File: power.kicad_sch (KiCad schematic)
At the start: 41 parts, among them J1 POWER_IN, J2 POWER_OUT, Q1 SUD50P10-43L-GE3, Q2 SUD50P10-43L-GE3, Q3 SUD50P10-43L-GE3, U12 +3V3@2A, U9 +5V@2A

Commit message: more cleanup and added notes for review
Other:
- note added: "ADD FERRITES?"
- note added: "DO WE HAVE AN INTERNAL TEMP SENSOR?"
- note added: "FUSE OUTPUTS"
- note added: "INCREASE BULK CAPACTORS AND GET 100V RATED"
- note added: "OR ADD CURRENT SENSOR"
- note removed: "These power..."

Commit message: DNP unused connectors for now
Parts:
- J2: now not fitted
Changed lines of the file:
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@@
 		(in_bom yes)
 		(on_board yes)
-		(dnp no)
+		(dnp yes)
 		(property "Reference" "J2"
 			(at 231.902 132.842 0)

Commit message: pcb review session notes
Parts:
- J2: now fitted
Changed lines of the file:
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@@
 	(text "ADD FERRITES?\n"
 		(exclude_from_sim no)
-		(at 28.5927 76.2834 0)
+		(at 17.526 68.58 0)
 		(effects
 			(font
@@
 	(text "OR ADD CURRENT SENSOR"
 		(exclude_from_sim no)
-		(at 199.898 166.878 0)
+		(at 180.086 162.56 0)
 		(effects
 			(font
@@
 	(text "INCREASE BULK CAPACTORS\nAND GET 100V RATED"
 		(exclude_from_sim no)
-		(at 123.19 74.93 0)
+		(at 132.842 40.386 0)
 		(effects
 			(font
@@
 		(in_bom yes)
 		(on_board yes)
-		(dnp yes)
+		(dnp no)
 		(property "Reference" "J2"
 			(at 231.902 132.842 0)

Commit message: major rework again after the meeting
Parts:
- removed C1, C11, C12, C13, C2, C3, C4: 0.1 uF, Capacitor_SMD:C_1206_3216Metric_Pad1.33x1.80mm_HandSolder, symbol Device:C
- removed C10, C5: 22 uF, Payload_PCB_v3.1:UCM1H220MCL1GS, symbol Device:C_Polarized_US
- removed D2, D3: BZT52C10-TP, Diode_SMD:D_SOD-123, symbol Device:D_Zener
- removed F2, F3: Fuse, Fuse:Fuseholder_Blade_Mini_Keystone_3568, symbol Device:Fuse
- removed JP1, JP2, JP3, JP4: SolderJumper_2_Open, Jumper:SolderJumper-2_P1.3mm_Open_RoundedPad1.0x1.5mm, symbol Jumper:SolderJumper_2_Open
- removed Q2, Q3: SUD50P10-43L-GE3, Package_TO_SOT_SMD:TO-252-2, symbol Device:Q_PMOS_GDS
- removed TP2: +BATT_IN, TestPoint:TestPoint_Pad_D2.0mm, symbol Connector:TestPoint
- removed TP3: +VDC_IN, TestPoint:TestPoint_Pad_D2.0mm, symbol Connector:TestPoint
- removed TP4, TP6: +12V_IN, TestPoint:TestPoint_Pad_D2.0mm, symbol Connector:TestPoint
- added C1: 22 uF, Capacitor_THT:CP_Radial_D10.0mm_P5.00mm, symbol Device:C_Polarized_US
- added D2, D3, D5: +12V, LED_SMD:LED_0805_2012Metric_Pad1.15x1.40mm_HandSolder, symbol Device:LED
- added Q2: MMBT3904, Package_TO_SOT_SMD:SOT-23, symbol Transistor_BJT:MMBT3904
- added R10, R8, R9: 45m, Resistor_SMD:R_1206_3216Metric_Pad1.30x1.75mm_HandSolder, symbol Device:R_US
- added R17: 511, Resistor_SMD:R_0603_1608Metric_Pad0.98x0.95mm_HandSolder, symbol Device:R_US
- added U3: LTC2990, Package_SO:MSOP-10_3x3mm_P0.5mm, symbol Sensor:LTC2990
- C9: value 0.1 uF -> 470p; footprint Capacitor_SMD:C_1206_3216Metric_Pad1.33x1.80mm_HandSolder -> Capacitor_SMD:C_0603_1608Metric_Pad1.08x0.95mm_HandSolder
- F1: footprint Fuse:Fuseholder_Blade_Mini_Keystone_3568 -> Fuse:Fuse_1210_3225Metric
- J1: footprint Connector_Molex:Molex_Mini-Fit_Jr_5569-06A2_2x03_P4.20mm_Horizontal -> Connector_Molex:Molex_Micro-Fit_3.0_43045-0200_2x01_P3.00mm_Horizontal; symbol Connector_Generic:Conn_02x03_Counter_Clockwise -> Connector_Generic:Conn_01x02; Manufacturer (none) -> Molex; Manufacturer Part Number (none) -> 0430450200; Vendor (none) -> Digikey; Vendor Part Number (none) -> WM1813-ND
- J2: footprint Connector_Molex:Molex_Mini-Fit_Jr_5569-12A2_2x06_P4.20mm_Horizontal -> Connector_Molex:Molex_Micro-Fit_3.0_43045-0600_2x03_P3.00mm_Horizontal; symbol Connector_Generic:Conn_02x06_Counter_Clockwise -> Connector_Generic:Conn_02x03_Top_Bottom; Manufacturer (none) -> Molex; Manufacturer Part Number (none) -> 0430450602; Vendor (none) -> Digikey; Vendor Part Number (none) -> WM1821-ND
- R3, R4: value 100k -> 511; footprint Resistor_SMD:R_0805_2012Metric_Pad1.20x1.40mm_HandSolder -> Resistor_SMD:R_0603_1608Metric_Pad0.98x0.95mm_HandSolder
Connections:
- net +12V: now also J2.4 (Pin_4), C1.1, R10.2, R17.2, R8.2, R9.2, U3.2 (V2); no longer D1.1 (K), J2.8 (Pin_8), J2.9 (Pin_9), Q1.3 (S)
- net +12V_IN: now also J1.2 (Pin_2); no longer J1.6 (Pin_6)
- net +3.3V: now also J2.6 (Pin_6), R4.2; no longer J2.11 (Pin_11)
- net +5V: now also J2.5 (Pin_5), R3.2; no longer J2.10 (Pin_10)
- net GND: now also C1.2, D2.1 (K), D3.1 (K), D5.1 (K), U3.5 (GND), U3.8 (ADR0), U3.9 (ADR1); no longer C9.1, J1.2 (Pin_2), J1.3 (Pin_3), J2.4 (Pin_4), J2.5 (Pin_5), J2.6 (Pin_6), R3.2, R4.2
- net at R4.1: now also D3.2 (A)
- net at R3.1: now also D2.2 (A)
- net +BATT: no longer names the net of C9.2
- net +BATT: now also Q2.1 (B), Q2.3 (C), U3.3 (V3); no longer J2.7 (Pin_7)
- removed net +BATT_IN: J1.5 (Pin_5)
- removed net VDC: J2.12 (Pin_12)
- new net: D5.2 (A), R17.1
- new net: C9.1, Q2.2 (E), U3.4 (V4)
- new net +12V_PROTECTED: D1.1 (K), Q1.3 (S), R10.1, R8.1, R9.1, U3.1 (V1)
- new net I2C0_SCL: U3.7 (SCL)
- new net I2C0_SDA: U3.6 (SDA)
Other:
- note added: "BULK CAPACITOR"
- note added: "CURRENT AND TEMPERATURE MONITOR"
- note removed: "+VDC is the servo voltage."
- note removed: "ADD FERRITES?"
- note removed: "Additional voltage input option or extra 40V input."
- note removed: "Bulk Decoupling"
- note removed: "DO WE HAVE AN INTERNAL TEMP SENSOR?"
- note removed: "FUSE OUTPUTS"
- note removed: "Fuse Protection"
- note removed: "INCREASE BULK CAPACTORS AND GET 100V RATED"
- note removed: "Note that these voltages are protected."
- note removed: "OR ADD CURRENT SENSOR"
- note removed: "Reverse-voltage protection"
- note removed: "The main power source is the +12V in. The other voltages are fed directly back out and are unused by any onboard components."
- moved on the sheet: D1, F1, Q1, R2, TP1, TP10, TP11, TP5, TP7, TP8, TP9, U12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

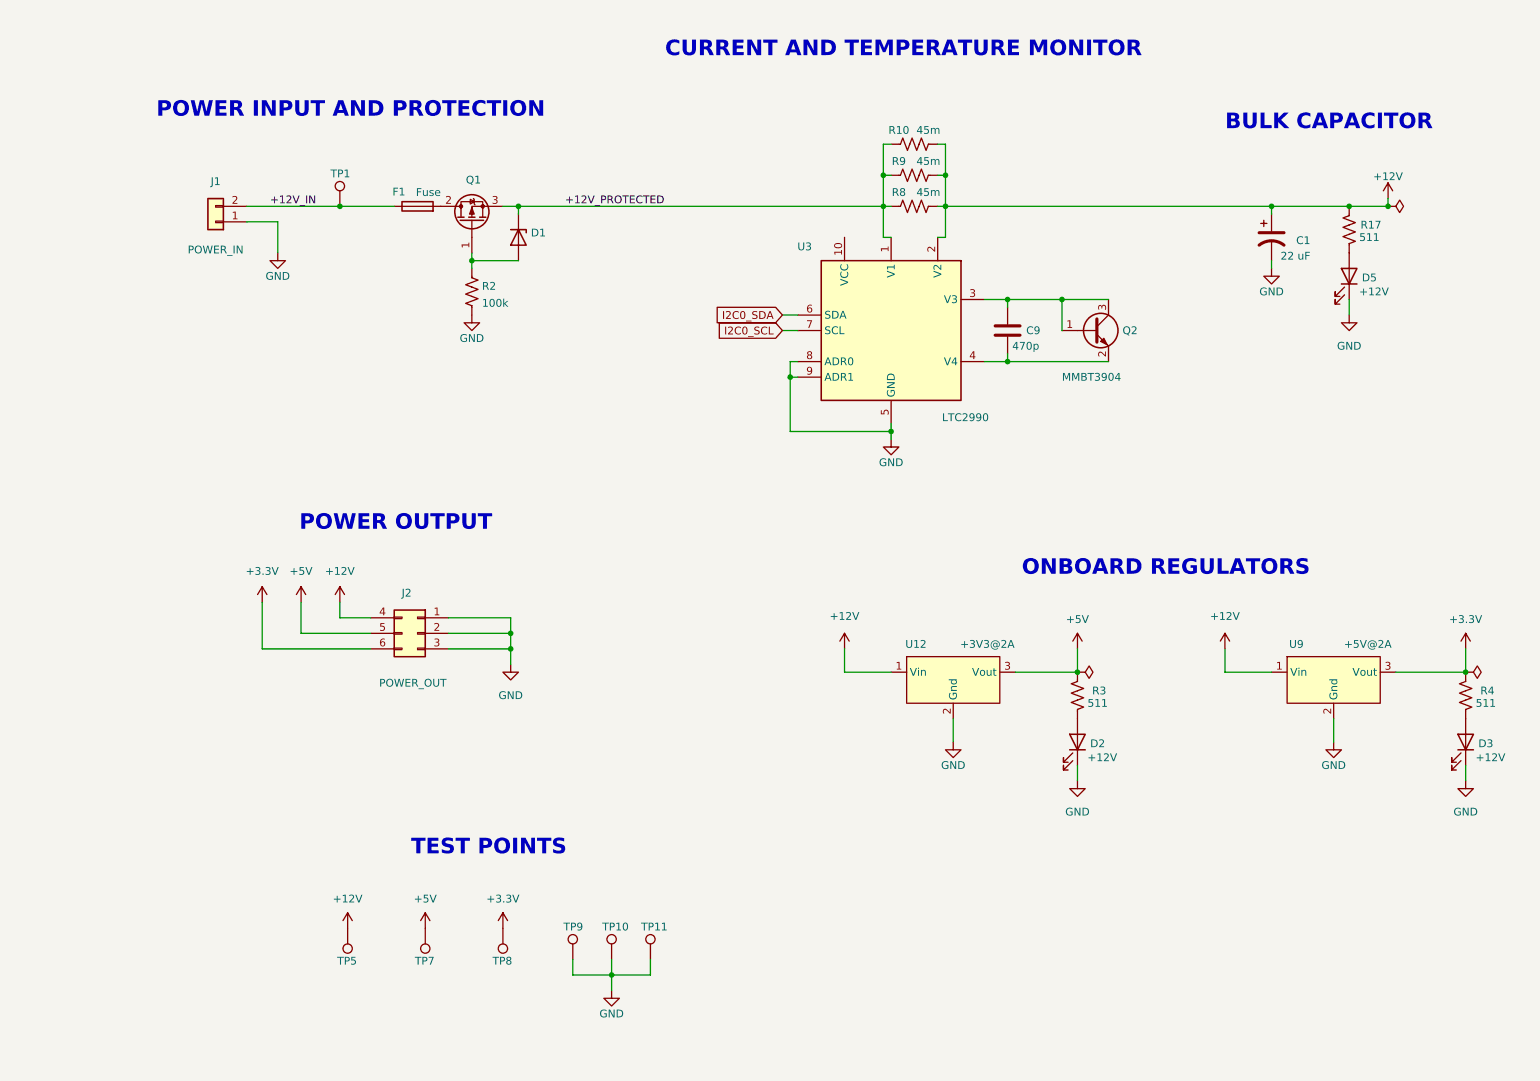
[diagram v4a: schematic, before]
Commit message: major finishing touches:     - major rework for v5.1     - silkscreen and stuff     - impednace for USB and CAN lines     - schematic comments     - symbol, footprint, and model library updates
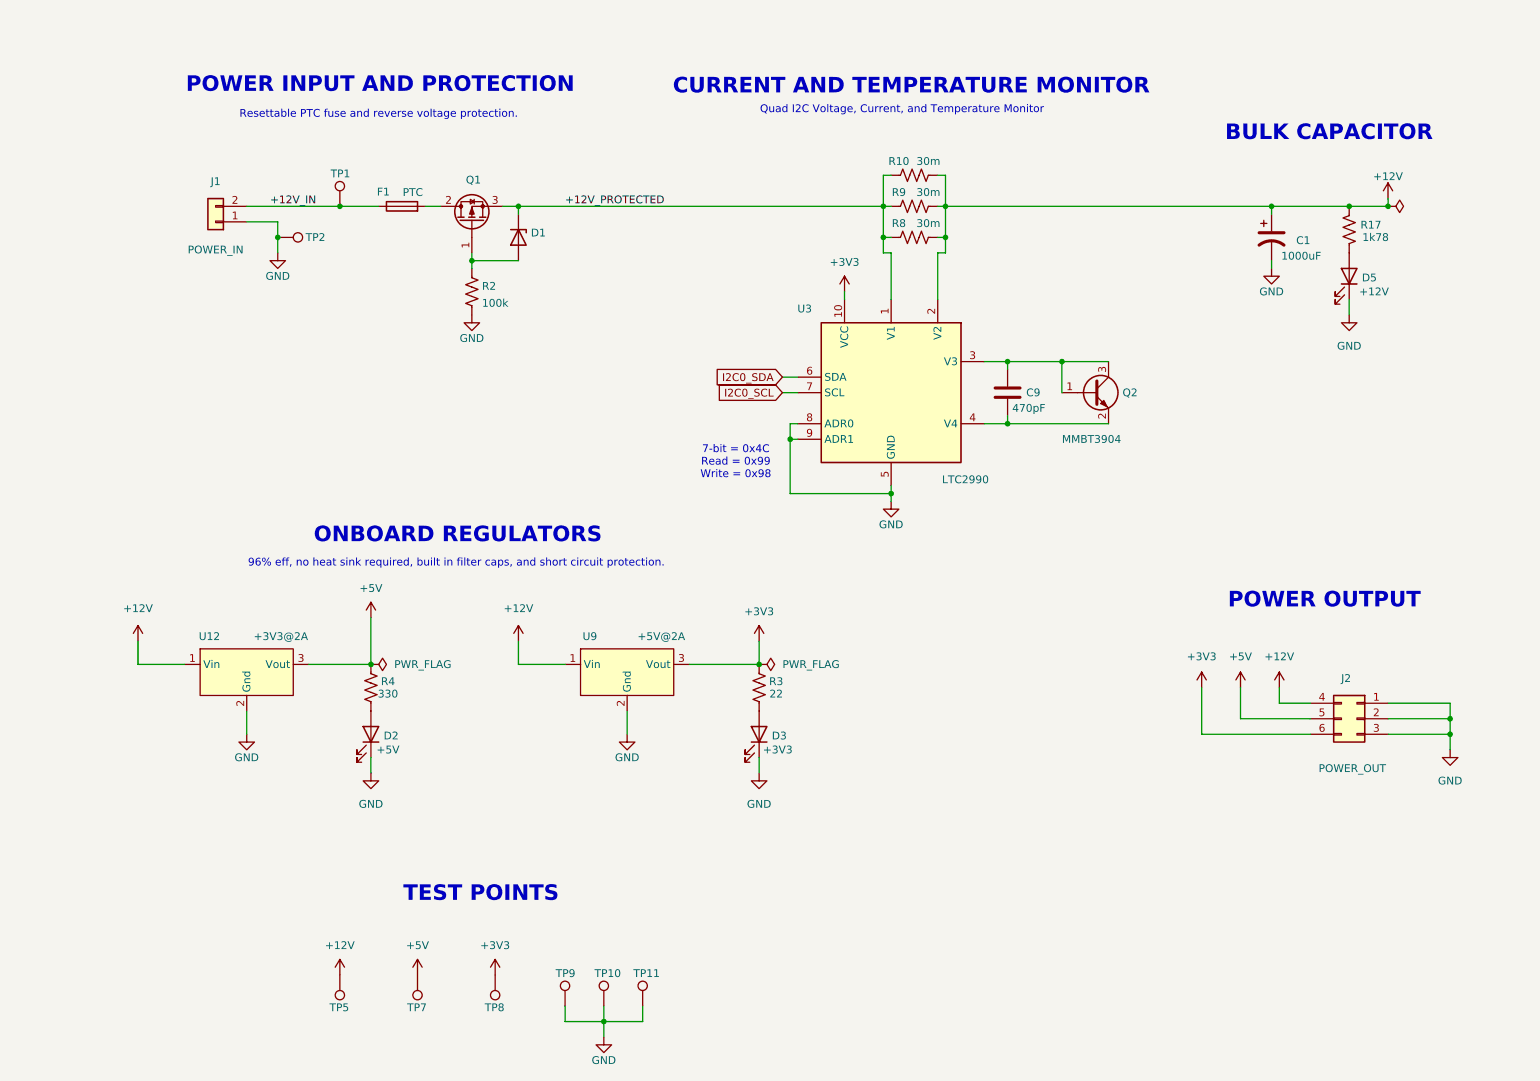
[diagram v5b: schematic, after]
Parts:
- added TP2: GND, TestPoint:TestPoint_Pad_D2.0mm, symbol Connector:TestPoint
- C1: value 22 uF -> 1000uF; Manufacturer (none) -> Nichicon; Manufacturer Part Number (none) -> UVR1E102MPD; Vendor (none) -> Digikey; Vendor Part Number (none) -> 493-1065-ND
- C9: value 470p -> 470pF; Manufacturer (none) -> KEMET; Manufacturer Part Number (none) -> C0603C471K5RACTU; Vendor (none) -> Digikey; Vendor Part Number (none) -> 399-C0603C471K5RACTUCT-ND
- D1: Manufacturer (none) -> MCC (Micro Commercial Components); Manufacturer Part Number (none) -> BZT52C10-TP; Vendor (none) -> Digikey; Vendor Part Number (none) -> BZT52C10-TPMSCT-ND
- D2: value +12V -> +5V; Manufacturer (none) -> Würth Elektronik; Manufacturer Part Number (none) -> 150080GS75000; Vendor (none) -> Digikey; Vendor Part Number (none) -> 732-4983-1-ND
- D3: value +12V -> +3V3; Manufacturer (none) -> Würth Elektronik; Manufacturer Part Number (none) -> 150080GS75000; Vendor (none) -> Digikey; Vendor Part Number (none) -> 732-4983-1-ND
- D5: Manufacturer (none) -> Würth Elektronik; Manufacturer Part Number (none) -> 150080GS75000; Vendor (none) -> Digikey; Vendor Part Number (none) -> 732-4983-1-ND
- F1: value Fuse -> PTC; Manufacturer (none) -> Littelfuse Inc.; Manufacturer Part Number (none) -> 1210L150/16WR; Vendor (none) -> Digikey; Vendor Part Number (none) -> F6135CT-ND
- Q1: symbol Device:Q_PMOS_GDS -> Transistor_FET:Q_PMOS_GDS; Manufacturer (none) -> Vishay Siliconix; Manufacturer Part Number (none) -> SUD50P10-43L-GE3; Vendor (none) -> Digikey; Vendor Part Number (none) -> SUD50P10-43L-GE3CT-ND
- Q2: Manufacturer (none) -> onsemi; Manufacturer Part Number (none) -> MMBT3904LT1G; Vendor (none) -> Digikey; Vendor Part Number (none) -> MMBT3904LT1GOSCT-ND
- R10, R8, R9: value 45m -> 30m; Manufacturer (none) -> Stackpole Electronics Inc; Manufacturer Part Number (none) -> CSR1206FT30L0; Vendor (none) -> Digikey; Vendor Part Number (none) -> 738-CSR1206FT30L0CT-ND
- R17: value 511 -> 1k78; Manufacturer (none) -> Stackpole Electronics Inc; Manufacturer Part Number (none) -> RNCP0603FTD1K78; Vendor (none) -> Digikey; Vendor Part Number (none) -> RNCP0603FTD1K78CT-ND
- R2: footprint Resistor_SMD:R_0805_2012Metric_Pad1.20x1.40mm_HandSolder -> Resistor_SMD:R_0603_1608Metric_Pad0.98x0.95mm_HandSolder; Manufacturer (none) -> Stackpole Electronics Inc; Manufacturer Part Number (none) -> RMCF0603FT100K; Vendor (none) -> Digikey; Vendor Part Number (none) -> RMCF0603FT100KCT-ND
- R3: value 511 -> 22; Manufacturer (none) -> Stackpole Electronics Inc; Manufacturer Part Number (none) -> RNCP0603FTD22R1; Vendor (none) -> Digikey; Vendor Part Number (none) -> RNCP0603FTD22R1CT-ND
- R4: value 511 -> 330; Manufacturer (none) -> Stackpole Electronics Inc; Manufacturer Part Number (none) -> RNCP0603FTD332R; Vendor (none) -> Digikey; Vendor Part Number (none) -> RNCP0603FTD332RCT-ND
- TP1: now left out of the parts list
- TP10, TP11, TP9: value +12V_IN -> GND; now left out of the parts list
- TP5: value +12V_IN -> +12V; now left out of the parts list
- TP7: value +12V_IN -> +5V; now left out of the parts list
- TP8: value +12V_IN -> +3V3; now left out of the parts list
- U12: symbol Regulators:173010542 -> symbols:TSR_2-2433; Manufacturer (none) -> Traco Power; Manufacturer Part Number (none) -> TSR 2-2433; Vendor (none) -> Digikey; Vendor Part Number (none) -> 1951-2426-ND
- U3: Manufacturer (none) -> Analog Devices Inc.; Manufacturer Part Number (none) -> LTC2990IMS#TRPBF; Vendor (none) -> Digikey; Vendor Part Number (none) -> 505-LTC2990IMS#TRPBFCT-ND
- U9: symbol Regulators:173010542 -> symbols:TSR_2-2450; Manufacturer (none) -> Traco Power; Manufacturer Part Number (none) -> TSR 2-2450; Vendor (none) -> Digikey; Vendor Part Number (none) -> 1951-2692-ND
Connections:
- net +5V: now also R4.2; no longer R3.2
- net GND: now also TP2.1
- net at R4.1: now also D2.2 (A); no longer D3.2 (A)
- net at R3.1: now also D3.2 (A); no longer D2.2 (A)
- net +3V3: now reaches U3.10 (VCC)
- net +3V3: now also J2.6 (Pin_6), R3.2, TP8.1, U9.3 (Vout)
- removed net +3.3V: J2.6 (Pin_6), R4.2, TP8.1, U9.3 (Vout)
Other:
- note added: "7-bit = 0x4C Read = 0x99 Write = 0x98"
- note added: "96% eff, no heat sink required, built in filter caps, and short circuit protection."
- note added: "Quad I2C Voltage, Current, and Temperature Monitor"
- note added: "Resettable PTC fuse and reverse voltage protection."
- company: WVU Unviersity Rover Challenge -> WVU Unviersity Rover Challenge (URC)
- moved on the sheet: C9, D2, D3, F1, J2, Q2, R10, R8, R9, TP10, TP11, TP5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

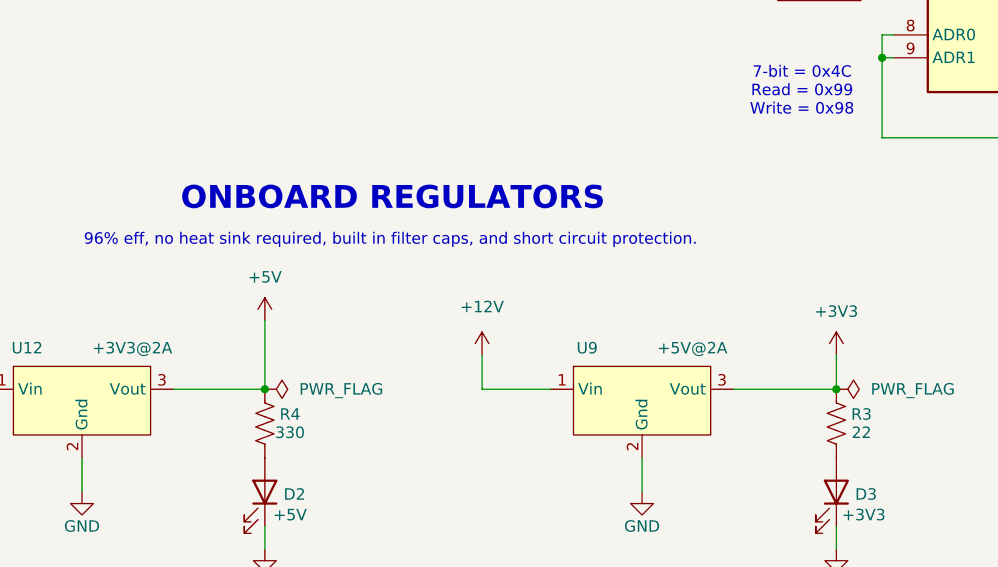
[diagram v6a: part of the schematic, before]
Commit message: swapped UART to USB from FTDI (out of stock) to MCP2200
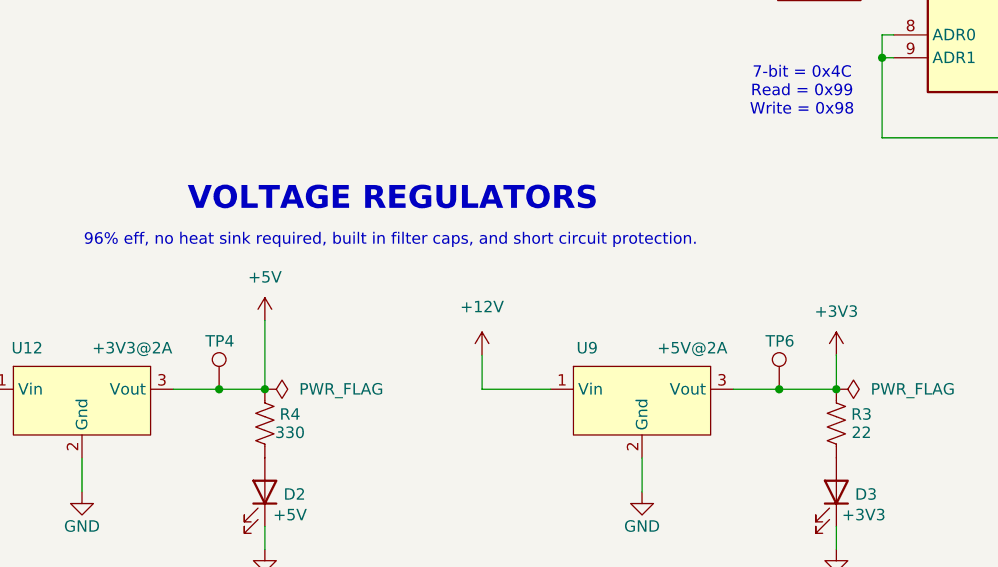
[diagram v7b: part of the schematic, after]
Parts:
- added TP4: +5V, TestPoint:TestPoint_Pad_D2.0mm, symbol Connector:TestPoint
- added TP6: +3V3, TestPoint:TestPoint_Pad_D2.0mm, symbol Connector:TestPoint
- U12, U9: footprint Payload_PCB_v3.1:CONV_TSR_2-2433 -> footprints:TSR_2-24xx
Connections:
- net +3V3: now also TP6.1
- net +5V: now also TP4.1
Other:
- note added: "VOLTAGE REGULATORS"
- note removed: "ONBOARD REGULATORS"

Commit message: added release documents for v5.1 (pending approval)
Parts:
- D1: Manufacturer MCC (Micro Commercial Components) -> MCC
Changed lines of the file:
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@@
 			)
 		)
-		(property "Manufacturer" "MCC (Micro Commercial Components)"
+		(property "Manufacturer" "MCC"
 			(at 100.33 58.42 90)
 			(effects
